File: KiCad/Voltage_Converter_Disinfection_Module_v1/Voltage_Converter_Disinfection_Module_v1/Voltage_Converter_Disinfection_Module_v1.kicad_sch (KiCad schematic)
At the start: 1 part, among them U1 LM317T

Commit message: feat: some progress for `Voltage_Converter_Disinfection_Module_v1`
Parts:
- added C1: 100n_50V, Capacitor_SMD:C_0402_1005Metric, symbol _C_0402:100n_50V
- added C2: 10u_25V, Capacitor_SMD:C_0603_1608Metric, symbol _C_0603:10u_25V
- added C3: 1u_50V, Capacitor_SMD:C_0805_2012Metric, symbol _C_0805:1u_50V
- added X1, X2: Conn_01x02_2.5mm_JST_S02B-XASS-1N-BN, Connector_JST:JST_XA_S02B-XASK-1N-BN_1x02_P2.50mm_Horizontal, symbol _Connector_JST:Conn_01x02_2.5mm_JST_S02B-XASS-1N-BN
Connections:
- net at U1.1 (ADJ): now also C2.1
- net +7.5V: now reaches U1.2 (VO)
- net +7.5V: now also C3.1, X2.1 (Pin_1)
- net +12V: now reaches U1.3 (VI)
- net +12V: now also C1.1, X1.2 (Pin_2)
- new net GND: C1.2, C2.2, C3.2, X1.1 (Pin_1), X2.2 (Pin_2)
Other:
- note added: "Input"
- note added: "Output"
- moved on the sheet: U1

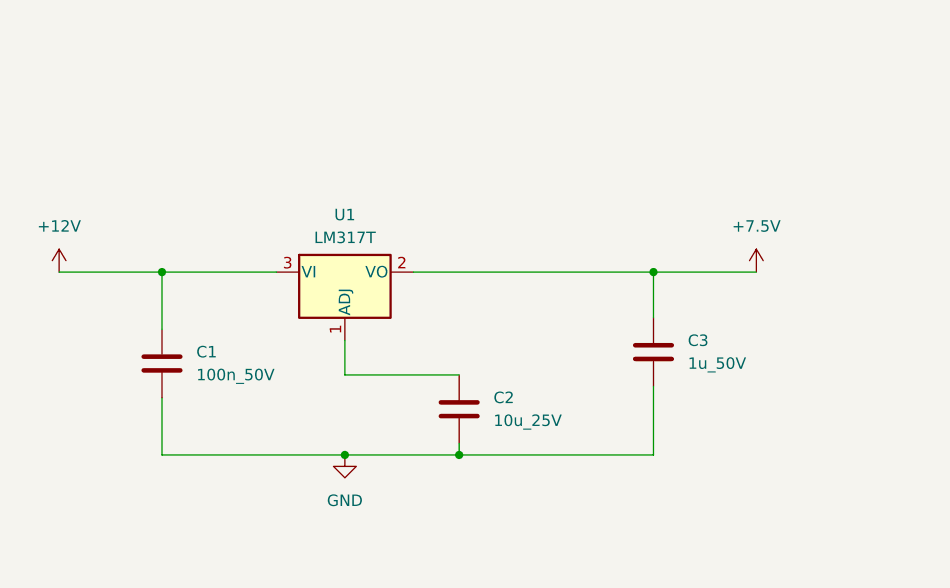
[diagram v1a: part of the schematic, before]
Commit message: feat: more progress on the `Voltage_Converter_Disinfection_Module_v1`
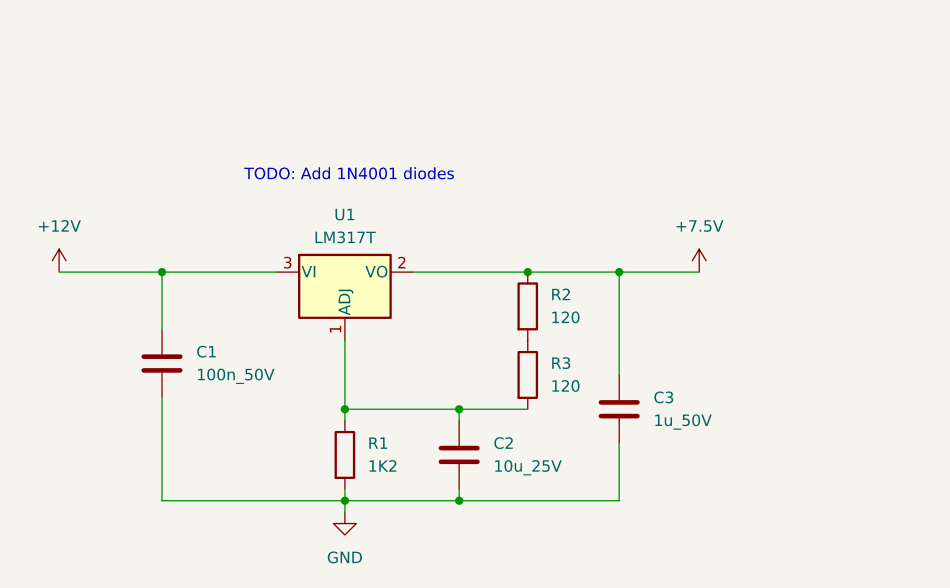
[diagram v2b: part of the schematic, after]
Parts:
- added R1: 1K2, Resistor_SMD:R_0603_1608Metric, symbol _R_0603:1K2
- added R2, R3: 120, Resistor_SMD:R_0603_1608Metric, symbol _R_0603:120
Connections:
- net +7.5V: now also R2.1
- net GND: now also R1.2
- net at C2.1, U1.1 (ADJ): now also R1.1, R3.2
- new net: R2.2, R3.1
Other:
- note added: "TODO: Add 1N4001 diodes"
- moved on the sheet: C2, C3

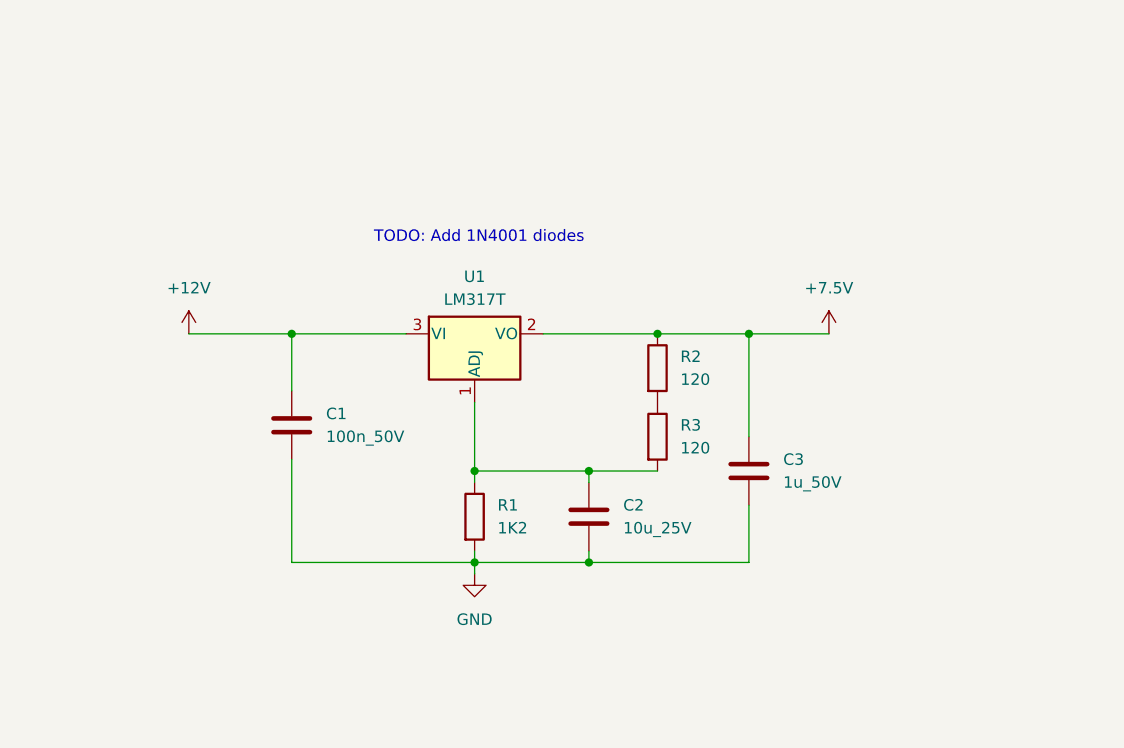
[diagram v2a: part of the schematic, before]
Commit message: feat: finished schematic for `Voltage_Converter_Disinfection_Module_v1`
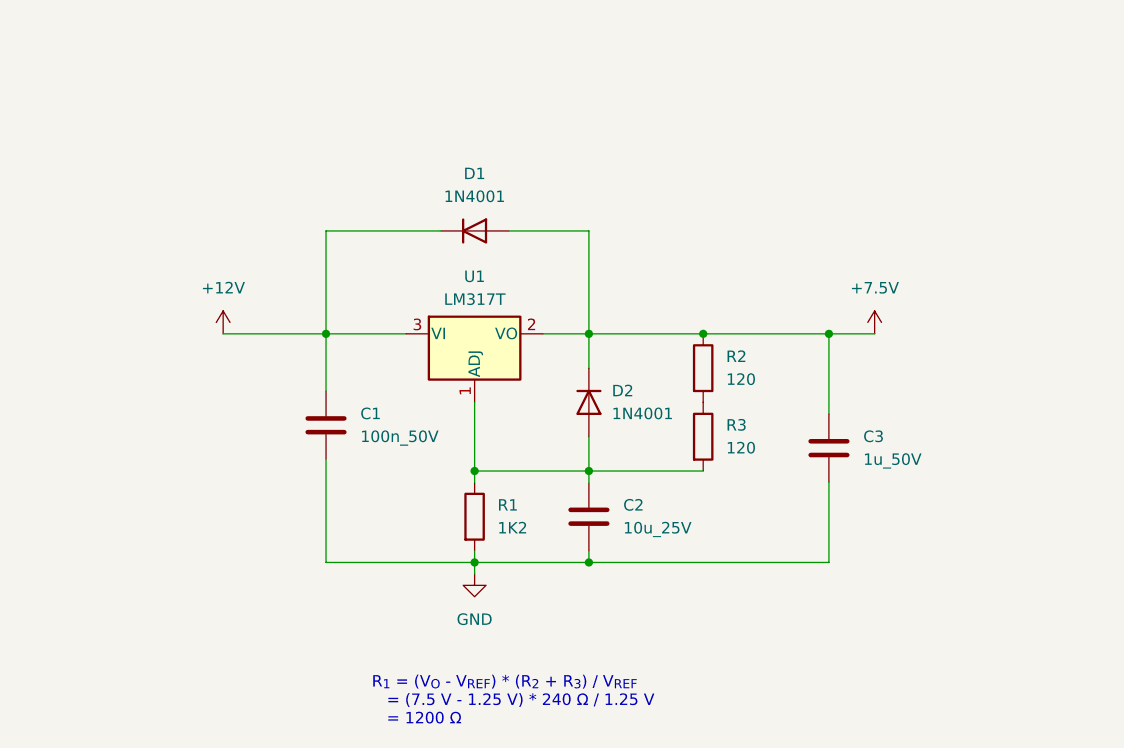
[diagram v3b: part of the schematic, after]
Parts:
- added D1, D2: 1N4001, Diode_SMD:D_SMA, symbol _Diode:1N4001
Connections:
- net +12V: now also D1.1 (K)
- net +7.5V: now also D1.2 (A), D2.1 (K)
- net at C2.1, R1.1, R3.2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: now also D2.2 (A)
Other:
- note added: "R_{1} = (V_{O} - V_{REF}) * (R_{2} + R_{3}) / V_{REF} = (7.5 V - 1.25 V) * 240 Ω / 1.25 V = 1200 Ω"
- note removed: "TODO: Add 1N4001 diodes"
- moved on the sheet: C1, C3, R2, R3

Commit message: chore: updated symbols for `Voltage_Converter_Disinfection_Module_v1`
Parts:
- C1, C2, C3: path_to_docs (none) -> Passive_Components/Capacitors/MLCC/Samsung_Electro-Mechanics
- U1: path_to_docs documents\Semiconductor\Power_Management\Linear_Voltage_Reg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 -> documents/Semiconductors/Power_Management/Linear_Voltage_Re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
- X1, X2: path_to_docs (none) -> Connectors/JST/XA_Connector
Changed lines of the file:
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@@
 			)
 		)
-		(property "path_to_docs" ""
+		(property "path_to_docs" "Passive_Components/Capacitors/MLCC/Samsung_Electro-Mechanics"
 			(at 146.05 91.44 0)
 			(effects
@@
 			)
 		)
+		(property "OC_CONRAD" ""
+			(at 172.72 83.82 0)
+			(effects
+				(font
+					(size 1.27 1.27)
+				)
+				(hide yes)
+			)
+		)
+		(property "OC_RS" ""
+			(at 172.72 83.82 0)
+			(effects
+				(font
+					(size 1.27 1.27)
+				)
+				(hide yes)
+			)
+		)
+		(property "path_to_docs" "Passive_Components/Capacitors/MLCC/Samsung_Electro-Mechanics"
+			(at 172.72 83.82 0)
+			(effects
+				(font
+					(size 1.27 1.27)
+				)
+				(hide yes)
+			)
+		)
 		(pin "2"
 		)
@@
 			)
 		)
-		(property "path_to_docs" "documents\\Semiconductor\\Power_Management\\Linear_Voltage_Regulator\\LM317T"
+		(property "path_to_docs" "documents/Semiconductors/Power_Management/Linear_Voltage_Regulators/LM317T"
 			(at 133.35 71.12 0)
 			(effects
@@
 			)
 		)
-		(property "Description" "Resistor 2K7 1% 100mW 75V 0603"
+		(property "Description" "Resistor 1K2 1% 100mW 75V 0603"
 			(at 133.35 91.44 0)
 			(effects
@@
 			)
 		)
+		(property "OC_CONRAD" ""
+			(at 116.84 81.28 0)
+			(effects
+				(font
+					(size 1.27 1.27)
+				)
+				(hide yes)
+			)
+		)
+		(property "OC_RS" ""
+			(at 116.84 81.28 0)
+			(effects
+				(font
+					(size 1.27 1.27)
+				)
+				(hide yes)
+			)
+		)
+		(property "path_to_docs" "Passive_Components/Capacitors/MLCC/Samsung_Electro-Mechanics"
+			(at 116.84 81.28 0)
+			(effects
+				(font
+					(size 1.27 1.27)
+				)
+				(hide yes)
+			)
+		)
 		(pin "1"
 		)
@@
 			)
 		)
+		(property "path_to_docs" "Connectors/JST/XA_Connector"
+			(at 40.64 33.02 0)
+			(effects
+				(font
+					(size 1.27 1.27)
+				)
+				(hide yes)
+			)
+		)
 		(pin "2"
 		)
@@
 			(at 233.68 26.67 0)
 			(effects
+				(font
+					(size 1.27 1.27)
+				)
+				(hide yes)
+			)
+		)
+		(property "path_to_docs" "Connectors/JST/XA_Connector"
+			(at 233.68 26.67 0)
+			(effects

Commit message: fix: updates `path_to_docs` for `LM317T`
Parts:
- U1: path_to_docs documents/Semiconductors/Power_Management/Linear_Voltage_Re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 -> Semiconductors/Power_Management/Linear_Voltage_Regulators/L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
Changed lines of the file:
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@@
 			)
 		)
-		(property "path_to_docs" "documents/Semiconductors/Power_Management/Linear_Voltage_Regulators/LM317T"
+		(property "path_to_docs" "Semiconductors/Power_Management/Linear_Voltage_Regulators/LM317T"
 			(at 133.35 71.12 0)
 			(effects
